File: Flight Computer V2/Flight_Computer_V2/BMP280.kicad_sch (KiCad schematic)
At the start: 3 parts, among them U4 BMP280

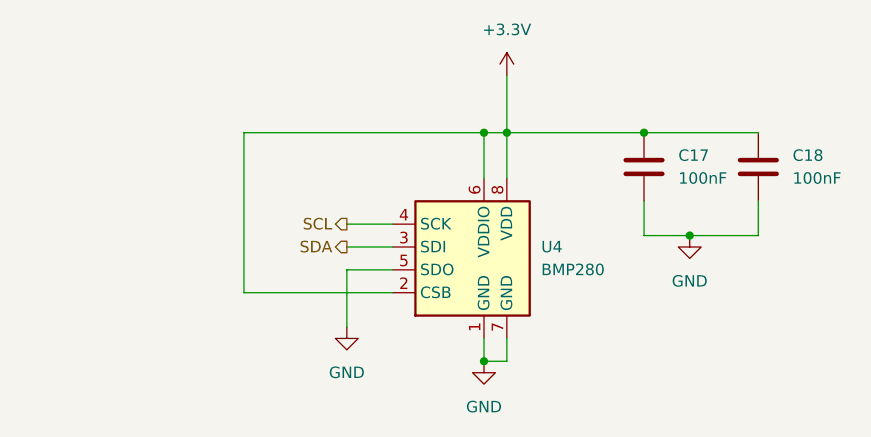
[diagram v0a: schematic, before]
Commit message: added more sensors to flight computer v2
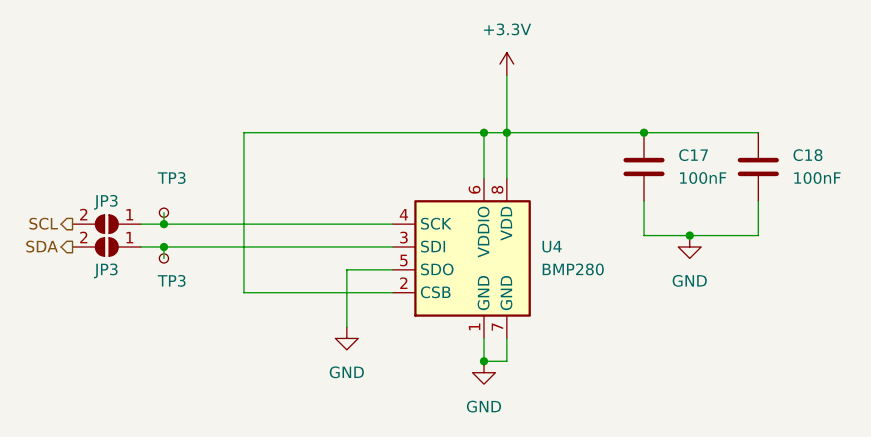
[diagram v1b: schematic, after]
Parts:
- added JP3 (x2): ~, symbol Jumper:SolderJumper_2_Open
- added TP3 (x2): TestPoint_Small, symbol Connector:TestPoint_Small
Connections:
- net SCL: now also JP3.2 (B); no longer U4.4 (SCK)
- net SDA: now also JP3.2 (B); no longer U4.3 (SDI)
- new net: JP3.1 (A), TP3.1, U4.4 (SCK)
- new net: JP3.1 (A), TP3.1, U4.3 (SDI)
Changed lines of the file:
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@@
   (junction (at 148.59 90.17) (diameter 0) (color 0 0 0 0)
   )
+  (junction (at 110.49 100.33) (diameter 0) (color 0 0 0 0)
+  )
   (junction (at 146.05 90.17) (diameter 0) (color 0 0 0 0)
   )
+  (junction (at 110.49 102.87) (diameter 0) (color 0 0 0 0)
+  )
   (junction (at 168.91 101.6) (diameter 0) (color 0 0 0 0)
   )
@@
     (stroke (width 0) (type default))
   )
+  (wire (pts (xy 110.49 102.87) (xy 107.95 102.87))
+    (stroke (width 0) (type default))
+  )
   (wire (pts (xy 148.59 83.82) (xy 148.59 90.17))
     (stroke (width 0) (type default))
@@
     (stroke (width 0) (type default))
   )
+  (wire (pts (xy 110.49 100.33) (xy 135.89 100.33))
+    (stroke (width 0) (type default))
+  )
   (wire (pts (xy 119.38 107.95) (xy 119.38 90.17))
     (stroke (width 0) (type default))
@@
     (stroke (width 0) (type default))
   )
-  (wire (pts (xy 130.81 102.87) (xy 135.89 102.87))
+  (wire (pts (xy 110.49 102.87) (xy 135.89 102.87))
+    (stroke (width 0) (type default))
+  )
+  (wire (pts (xy 110.49 99.06) (xy 110.49 100.33))
     (stroke (width 0) (type default))
   )
@@
     (stroke (width 0) (type default))
   )
-  (wire (pts (xy 130.81 100.33) (xy 135.89 100.33))
+  (wire (pts (xy 110.49 104.14) (xy 110.49 102.87))
     (stroke (width 0) (type default))
   )
@@
     (stroke (width 0) (type default))
   )
-  (hierarchical_label "SCL" (shape output) (at 130.81 100.33 180) (fields_autoplaced)
+  (wire (pts (xy 107.95 100.33) (xy 110.49 100.33))
+    (stroke (width 0) (type default))
+  )
+  (hierarchical_label "SDA" (shape output) (at 100.33 102.87 180) (fields_autoplaced)
     (effects (font (size 1.27 1.27)) (justify right))
   )
-  (hierarchical_label "SDA" (shape output) (at 130.81 102.87 180) (fields_autoplaced)
+  (hierarchical_label "SCL" (shape output) (at 100.33 100.33 180) (fields_autoplaced)
     (effects (font (size 1.27 1.27)) (justify right))
+  )
+  (symbol (lib_id "Connector:TestPoint_Small") (at 110.49 99.06 180) (unit 1)
+    (in_bom yes) (on_board yes) (dnp no)
+    (property "Reference" "TP3" (at 113.03 95.25 0)
+      (effects (font (size 1.27 1.27)) (justify left))
+    )
+    (property "Value" "TestPoint_Small" (at 109.22 97.79 0)
+      (effects (font (size 1.27 1.27)) (justify left) hide)
+    )
+    (property "Footprint" "" (at 105.41 99.06 0)
+      (effects (font (size 1.27 1.27)) hide)
+    )
+    (property "Datasheet" "~" (at 105.41 99.06 0)
+      (effects (font (size 1.27 1.27)) hide)
+    )
+    (pin "1")
+    (instances
+      (project "Flight_Computer_V2"
+        (path "/39d7ebb3-b69d-4ae9-8f55-c9acfe77d345/18b8eda5-ab3e-431c-bc45-74a94283215a"
+          (reference "TP3") (unit 1)
+        )
+        (path "/39d7ebb3-b69d-4ae9-8f55-c9acfe77d345/36f68de3-e25f-423d-b7f8-c15e88151435"
+          (reference "TP4") (unit 1)
+        )
+        (path "/39d7ebb3-b69d-4ae9-8f55-c9acfe77d345/728ff691-86aa-4406-a714-359017417c15"
+          (reference "TP12") (unit 1)
+        )
+        (path "/39d7ebb3-b69d-4ae9-8f55-c9acfe77d345/de413d1f-8d39-42d8-b833-6419d9c73587"
+          (reference "TP13") (unit 1)
+        )
+        (path "/39d7ebb3-b69d-4ae9-8f55-c9acfe77d345/806e3fbd-cca2-40cb-b727-86767e32e959"
+          (reference "TP14") (unit 1)
+        )
+        (path "/39d7ebb3-b69d-4ae9-8f55-c9acfe77d345/5302a5ff-4c5a-40f5-8b82-1f5be512d366"
+          (reference "TP15") (unit 1)
+        )
+        (path "/39d7ebb3-b69d-4ae9-8f55-c9acfe77d345/b1bb6dfd-0d07-44b6-b0d1-16713468007b"
+          (reference "TP25") (unit 1)
+        )
+      )
+    )
+  )
+  (symbol (lib_id "Jumper:SolderJumper_2_Open") (at 104.14 100.33 180) (unit 1)
+    (in_bom yes) (on_board yes) (dnp no)
+    (property "Reference" "JP3" (at 104.14 97.79 0)
+      (effects (font (size 1.27 1.27)))
+    )
+    (property "Value" "~" (at 104.14 104.14 0)
+      (effects (font (size 1.27 1.27)))
+    )
+    (property "Footprint" "" (at 104.14 100.33 0)
+      (effects (font (size 1.27 1.27)) hide)
+    )
+    (property "Datasheet" "~" (at 104.14 100.33 0)
+      (effects (font (size 1.27 1.27)) hide)
+    )
+    (pin "1")
+    (pin "2")
+    (instances
+      (project "Flight_Computer_V2"
+        (path "/39d7ebb3-b69d-4ae9-8f55-c9acfe77d345/18b8eda5-ab3e-431c-bc45-74a94283215a"
+          (reference "JP3") (unit 1)
+        )
+        (path "/39d7ebb3-b69d-4ae9-8f55-c9acfe77d345/36f68de3-e25f-423d-b7f8-c15e88151435"
+          (reference "JP4") (unit 1)
+        )
+        (path "/39d7ebb3-b69d-4ae9-8f55-c9acfe77d345/728ff691-86aa-4406-a714-359017417c15"
+          (reference "JP14") (unit 1)
+        )
+        (path "/39d7ebb3-b69d-4ae9-8f55-c9acfe77d345/de413d1f-8d39-42d8-b833-6419d9c73587"
+          (reference "JP15") (unit 1)
+        )
+        (path "/39d7ebb3-b69d-4ae9-8f55-c9acfe77d345/806e3fbd-cca2-40cb-b727-86767e32e959"
+          (reference "JP16") (unit 1)
+        )
+        (path "/39d7ebb3-b69d-4ae9-8f55-c9acfe77d345/5302a5ff-4c5a-40f5-8b82-1f5be512d366"
+          (reference "JP17") (unit 1)
+        )
+        (path "/39d7ebb3-b69d-4ae9-8f55-c9acfe77d345/b1bb6dfd-0d07-44b6-b0d1-16713468007b"
+          (reference "JP27") (unit 1)
+        )
+      )
+    )
   )
   (symbol (lib_id "power:GND") (at 168.91 101.6 0) (unit 1)
@@
     )
   )
+  (symbol (lib_id "Jumper:SolderJumper_2_Open") (at 104.14 102.87 180) (unit 1)
+    (in_bom yes) (on_board yes) (dnp no)
+    (property "Reference" "JP3" (at 104.14 105.41 0)
+      (effects (font (size 1.27 1.27)))
+    )
+    (property "Value" "~" (at 104.14 106.68 0)
+      (effects (font (size 1.27 1.27)))
+    )
+    (property "Footprint" "" (at 104.14 102.87 0)
+      (effects (font (size 1.27 1.27)) hide)
+    )
+    (property "Datasheet" "~" (at 104.14 102.87 0)
+      (effects (font (size 1.27 1.27)) hide)
+    )
+    (pin "1")
+    (pin "2")
+    (instances
+      (project "Flight_Computer_V2"
+        (path "/39d7ebb3-b69d-4ae9-8f55-c9acfe77d345/18b8eda5-ab3e-431c-bc45-74a94283215a"
+          (reference "JP3") (unit 1)
+        )
+        (path "/39d7ebb3-b69d-4ae9-8f55-c9acfe77d345/36f68de3-e25f-423d-b7f8-c15e88151435"
+          (reference "JP4") (unit 1)
+        )
+        (path "/39d7ebb3-b69d-4ae9-8f55-c9acfe77d345/728ff691-86aa-4406-a714-359017417c15"
+          (reference "JP14") (unit 1)
+        )
+        (path "/39d7ebb3-b69d-4ae9-8f55-c9acfe77d345/de413d1f-8d39-42d8-b833-6419d9c73587"
+          (reference "JP15") (unit 1)
+        )
+        (path "/39d7ebb3-b69d-4ae9-8f55-c9acfe77d345/806e3fbd-cca2-40cb-b727-86767e32e959"
+          (reference "JP16") (unit 1)
+        )
+        (path "/39d7ebb3-b69d-4ae9-8f55-c9acfe77d345/5302a5ff-4c5a-40f5-8b82-1f5be512d366"
+          (reference "JP17") (unit 1)
+        )
+        (path "/39d7ebb3-b69d-4ae9-8f55-c9acfe77d345/b1bb6dfd-0d07-44b6-b0d1-16713468007b"
+          (reference "JP26") (unit 1)
+        )
+      )
+    )
+  )
   (symbol (lib_id "power:+3.3V") (at 148.59 83.82 0) (unit 1)
     (in_bom yes) (on_board yes) (dnp no)
@@
         )
       )
+    )
+  )
+  (symbol (lib_id "Connector:TestPoint_Small") (at 110.49 104.14 180) (unit 1)
+    (in_bom yes) (on_board yes) (dnp no)
+    (property "Reference" "TP3" (at 113.03 106.68 0)
+      (effects (font (size 1.27 1.27)) (justify left))
+    )
+    (property "Value" "TestPoint_Small" (at 109.22 102.87 0)
+      (effects (font (size 1.27 1.27)) (justify left) hide)
+    )
+    (property "Footprint" "" (at 105.41 104.14 0)
+      (effects (font (size 1.27 1.27)) hide)
+    )
+    (property "Datasheet" "~" (at 105.41 104.14 0)
+      (effects (font (size 1.27 1.27)) hide)
+    )
+    (pin "1")
+    (instances
+      (project "Flight_Computer_V2"
+        (path "/39d7ebb3-b69d-4ae9-8f55-c9acfe77d345/18b8eda5-ab3e-431c-bc45-74a94283215a"
+          (reference "TP3") (unit 1)
+        )
+        (path "/39d7ebb3-b69d-4ae9-8f55-c9acfe77d345/36f68de3-e25f-423d-b7f8-c15e88151435"
+          (reference "TP4") (unit 1)
+        )
+        (path "/39d7ebb3-b69d-4ae9-8f55-c9acfe77d345/728ff691-86aa-4406-a714-359017417c15"
+          (reference "TP12") (unit 1)
+        )
+        (path "/39d7ebb3-b69d-4ae9-8f55-c9acfe77d345/de413d1f-8d39-42d8-b833-6419d9c73587"
+          (reference "TP13") (unit 1)
+        )
+        (path "/39d7ebb3-b69d-4ae9-8f55-c9acfe77d345/806e3fbd-cca2-40cb-b727-86767e32e959"
+          (reference "TP14") (unit 1)
+        )
+        (path "/39d7ebb3-b69d-4ae9-8f55-c9acfe77d345/5302a5ff-4c5a-40f5-8b82-1f5be512d366"
+          (reference "TP15") (unit 1)
+        )
+        (path "/39d7ebb3-b69d-4ae9-8f55-c9acfe77d345/b1bb6dfd-0d07-44b6-b0d1-16713468007b"
+          (reference "TP24") (unit 1)
+        )
+      )

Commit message: finalized schematic, added datasheets, and pdf of schematic
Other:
- company: (none) -> By: Dylan Haussecker
- title: (none) -> Avionics Flight Computer
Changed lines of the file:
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@@
 (kicad_sch (version 20230121) (generator eeschema)
   (paper "A4")
+  (title_block
+    (title "Avionics Flight Computer")
+    (date "2023-09-04")
+    (rev "1.0")
+    (company "By: Dylan Haussecker")
+  )
   (junction (at 163.83 90.17) (diameter 0) (color 0 0 0 0)
   )

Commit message: updated pcb
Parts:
- C17, C18: footprint (none) -> Capacitor_SMD:C_0402_1005Metric
- JP3: footprint (none) -> Jumper:SolderJumper-2_P1.3mm_Open_Pad1.0x1.5mm
- TP3: footprint (none) -> TestPoint:TestPoint_Pad_D1.0mm
- renumbered U4 to U44
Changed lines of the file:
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@@
       (effects (font (size 1.27 1.27)) (justify left) hide)
     )
-    (property "Footprint" "" (at 105.41 99.06 0)
+    (property "Footprint" "TestPoint:TestPoint_Pad_D1.0mm" (at 105.41 99.06 0)
       (effects (font (size 1.27 1.27)) hide)
     )
@@
       (effects (font (size 1.27 1.27)))
     )
-    (property "Footprint" "" (at 104.14 100.33 0)
+    (property "Footprint" "Jumper:SolderJumper-2_P1.3mm_Open_Pad1.0x1.5mm" (at 104.14 100.33 0)
       (effects (font (size 1.27 1.27)) hide)
     )
@@
   (symbol (lib_id "power:GND") (at 168.91 101.6 0) (unit 1)
     (in_bom yes) (on_board yes) (dnp no) (fields_autoplaced)
-    (property "Reference" "#PWR025" (at 168.91 107.95 0)
+    (property "Reference" "#PWR0111" (at 168.91 107.95 0)
       (effects (font (size 1.27 1.27)) hide)
     )
@@
       (project "Flight_Computer_V2"
         (path "/39d7ebb3-b69d-4ae9-8f55-c9acfe77d345/b1bb6dfd-0d07-44b6-b0d1-16713468007b"
+          (reference "#PWR0111") (unit 1)
+        )
+      )
+      (project "avionics_flight_computer"
+        (path "/b1d299c5-d712-4abd-abfc-85bf9dc0241e/69efb283-841e-4331-9a86-1fe2d1492264"
           (reference "#PWR025") (unit 1)
         )
       )
-      (project "avionics_flight_computer"
-        (path "/b1d299c5-d712-4abd-abfc-85bf9dc0241e/69efb283-841e-4331-9a86-1fe2d1492264"
-          (reference "#PWR025") (unit 1)
-        )
-      )
     )
   )
@@
       (effects (font (size 1.27 1.27)) (justify left))
     )
-    (property "Footprint" "" (at 177.4952 97.79 0)
+    (property "Footprint" "Capacitor_SMD:C_0402_1005Metric" (at 177.4952 97.79 0)
       (effects (font (size 1.27 1.27)) hide)
     )
@@
   (symbol (lib_id "power:GND") (at 130.81 111.76 0) (unit 1)
     (in_bom yes) (on_board yes) (dnp no) (fields_autoplaced)
-    (property "Reference" "#PWR024" (at 130.81 118.11 0)
+    (property "Reference" "#PWR0112" (at 130.81 118.11 0)
       (effects (font (size 1.27 1.27)) hide)
     )
@@
       (project "Flight_Computer_V2"
         (path "/39d7ebb3-b69d-4ae9-8f55-c9acfe77d345/b1bb6dfd-0d07-44b6-b0d1-16713468007b"
+          (reference "#PWR0112") (unit 1)
+        )
+      )
+      (project "avionics_flight_computer"
+        (path "/b1d299c5-d712-4abd-abfc-85bf9dc0241e/69efb283-841e-4331-9a86-1fe2d1492264"
           (reference "#PWR024") (unit 1)
         )
       )
-      (project "avionics_flight_computer"
-        (path "/b1d299c5-d712-4abd-abfc-85bf9dc0241e/69efb283-841e-4331-9a86-1fe2d1492264"
-          (reference "#PWR024") (unit 1)
-        )
-      )
     )
   )
   (symbol (lib_id "power:GND") (at 146.05 115.57 0) (unit 1)
     (in_bom yes) (on_board yes) (dnp no) (fields_autoplaced)
-    (property "Reference" "#PWR023" (at 146.05 121.92 0)
+    (property "Reference" "#PWR0110" (at 146.05 121.92 0)
       (effects (font (size 1.27 1.27)) hide)
     )
@@
       (project "Flight_Computer_V2"
         (path "/39d7ebb3-b69d-4ae9-8f55-c9acfe77d345/b1bb6dfd-0d07-44b6-b0d1-16713468007b"
+          (reference "#PWR0110") (unit 1)
+        )
+      )
+      (project "avionics_flight_computer"
+        (path "/b1d299c5-d712-4abd-abfc-85bf9dc0241e/69efb283-841e-4331-9a86-1fe2d1492264"
           (reference "#PWR023") (unit 1)
         )
       )
-      (project "avionics_flight_computer"
-        (path "/b1d299c5-d712-4abd-abfc-85bf9dc0241e/69efb283-841e-4331-9a86-1fe2d1492264"
-          (reference "#PWR023") (unit 1)
-        )
-      )
     )
   )
@@
       (effects (font (size 1.27 1.27)) (justify left))
     )
-    (property "Footprint" "" (at 164.7952 97.79 0)
+    (property "Footprint" "Capacitor_SMD:C_0402_1005Metric" (at 164.7952 97.79 0)
       (effects (font (size 1.27 1.27)) hide)
     )
@@
   (symbol (lib_id "Sensor_Pressure:BMP280") (at 146.05 105.41 0) (unit 1)
     (in_bom yes) (on_board yes) (dnp no) (fields_autoplaced)
-    (property "Reference" "U4" (at 152.4 102.87 0)
+    (property "Reference" "U44" (at 152.4 102.87 0)
       (effects (font (size 1.27 1.27)) (justify left))
     )
@@
       (project "Flight_Computer_V2"
         (path "/39d7ebb3-b69d-4ae9-8f55-c9acfe77d345/b1bb6dfd-0d07-44b6-b0d1-16713468007b"
-          (reference "U4") (unit 1)
+          (reference "U44") (unit 1)
         )
       )
@@
       (effects (font (size 1.27 1.27)))
     )
-    (property "Footprint" "" (at 104.14 102.87 0)
+    (property "Footprint" "Jumper:SolderJumper-2_P1.3mm_Open_Pad1.0x1.5mm" (at 104.14 102.87 0)
       (effects (font (size 1.27 1.27)) hide)
     )
@@
   (symbol (lib_id "power:+3.3V") (at 148.59 83.82 0) (unit 1)
     (in_bom yes) (on_board yes) (dnp no)
-    (property "Reference" "#PWR021" (at 148.59 87.63 0)
+    (property "Reference" "#PWR0109" (at 148.59 87.63 0)
       (effects (font (size 1.27 1.27)) hide)
     )
@@
       (project "Flight_Computer_V2"
         (path "/39d7ebb3-b69d-4ae9-8f55-c9acfe77d345/b1bb6dfd-0d07-44b6-b0d1-16713468007b"
-          (reference "#PWR021") (unit 1)
+          (reference "#PWR0109") (unit 1)
         )
       )
@@
       (effects (font (size 1.27 1.27)) (justify left) hide)
     )
-    (property "Footprint" "" (at 105.41 104.14 0)
-      (effects (font (size 1.27 1.27)) hide)
-    )
+    (property "Footprint" "TestPoint:TestPoint_Pad_D1.0mm" (at 105.41 104.14 0)
+      (effects (font (size 1.27 1.27)) hide)
+    )
